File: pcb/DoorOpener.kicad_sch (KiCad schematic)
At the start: 8 parts, among them J1 Serial, SW1 POWER, SW2 Button, U2 ESP-01v090

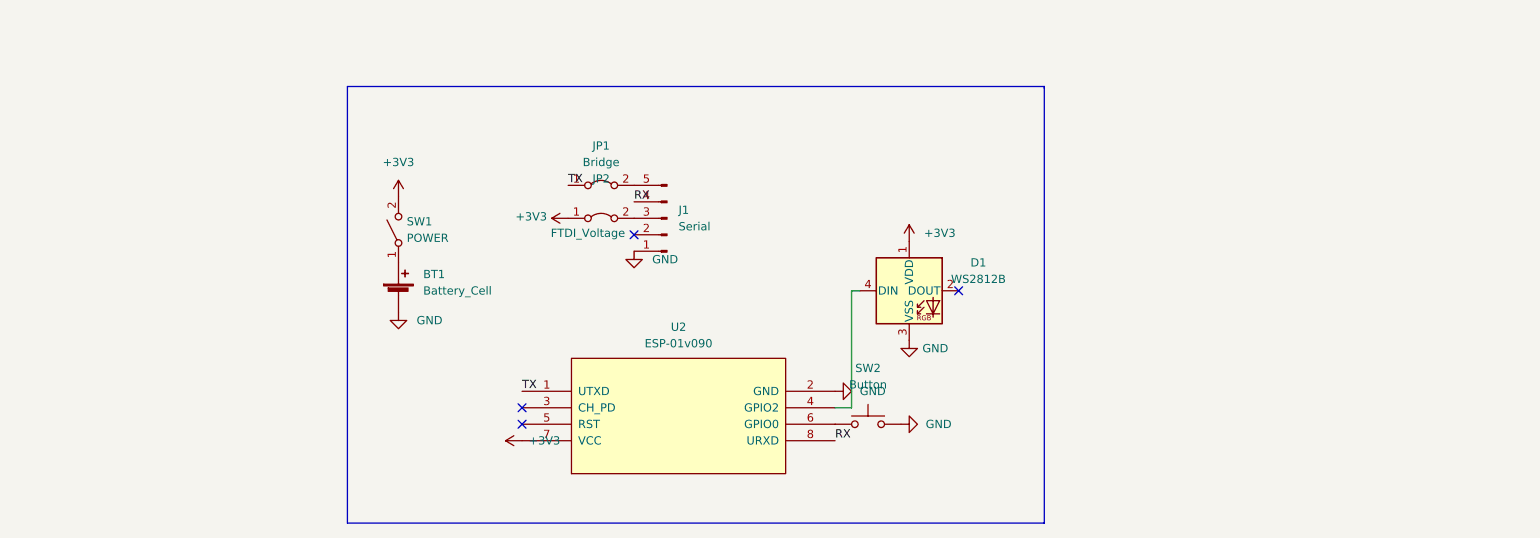
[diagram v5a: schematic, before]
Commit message: PCB: Add station module
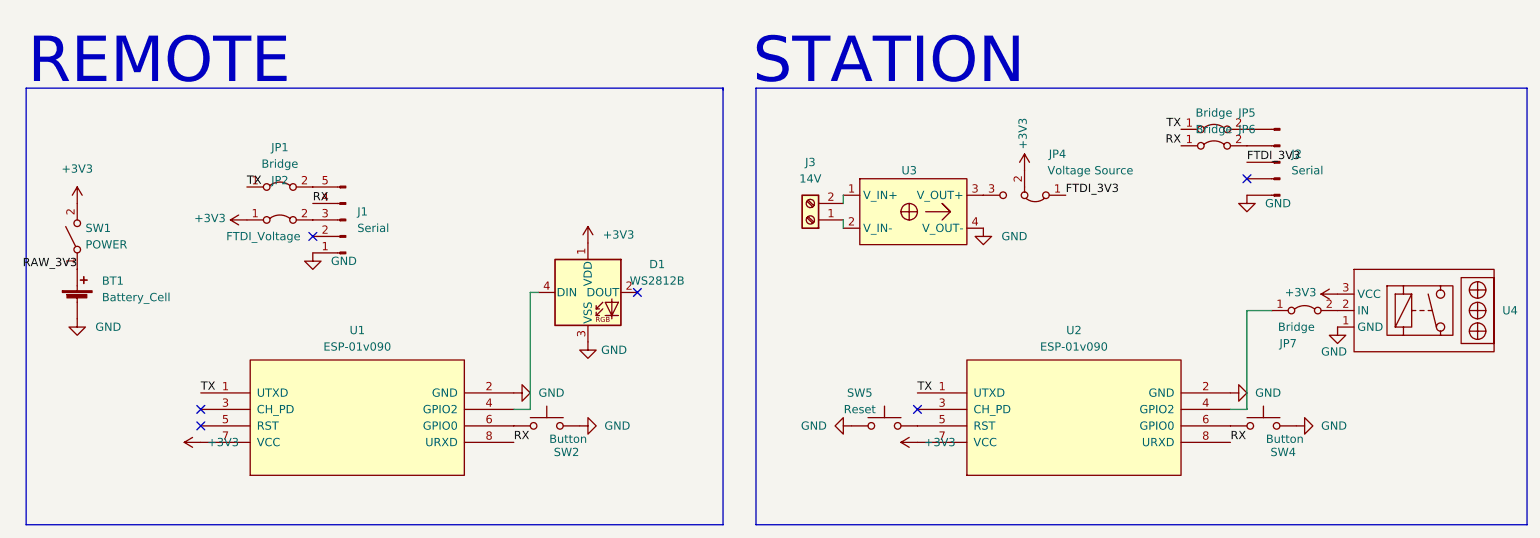
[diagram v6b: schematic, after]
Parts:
- added J2: Serial, Connector_PinHeader_2.54mm:PinHeader_1x05_P2.54mm_Horizontal, symbol Connector:Conn_01x05_Male
- added J3: 14V, TerminalBlock_Phoenix:TerminalBlock_Phoenix_MPT-0,5-2-2.54_1x02_P2.54mm_Horizontal, symbol Connector:Screw_Terminal_01x02
- added JP4: Voltage Source, Connector_PinHeader_2.54mm:PinHeader_1x03_P2.54mm_Vertical, symbol Jumper:Jumper_3_Bridged12
- added JP5, JP6, JP7: Bridge, Resistor_THT:R_Axial_DIN0204_L3.6mm_D1.6mm_P5.08mm_Horizontal, symbol Jumper:Jumper_2_Bridged
- added SW4: Button, Button_Switch_THT:SW_PUSH_6mm_H4.3mm, symbol Switch:SW_Push
- added SW5: Reset, Button_Switch_THT:SW_PUSH_6mm_H4.3mm, symbol Switch:SW_Push
- added U2: ESP-01v090, ESP8266:ESP-01, symbol ESP8266:ESP-01v090
- added U3: dcdc, dcdc:dcdc, symbol dcdc:dcdc
- added U4: relais_module, relais_module:relais_module, symbol relais_module:relais_module
- renumbered U2 to U1
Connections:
- net +3V3: now also JP4.2 (C), U2.7 (VCC), U4.3 (VCC)
- net GND: now also J2.1 (Pin_1), SW4.2, SW5.2, U2.2 (GND), U3.4 (V_OUT-), U4.1 (GND)
- net RX: now also JP6.1 (A), U2.8 (URXD)
- net TX: now also JP5.1 (A), U2.1 (UTXD)
- net RAW_3V3: now reaches BT1.1 (+), SW1.1 (A)
- new net: JP7.2 (B), U4.2 (IN)
- new net: JP7.1 (A), U2.4 (GPIO2)
- new net: SW4.1, U2.6 (GPIO0)
- new net: SW5.1, U2.5 (RST)
- new net: J2.5 (Pin_5), JP5.2 (B)
- new net: J3.1 (Pin_1), U3.2 (V_IN-)
- new net: J3.2 (Pin_2), U3.1 (V_IN+)
- new net: J2.4 (Pin_4), JP6.2 (B)
- new net: JP4.3 (B), U3.3 (V_OUT+)
- new net FTDI_3V3: J2.3 (Pin_3), JP4.1 (A)
- no-connect marks 4 -> 6
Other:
- note added: "REMOTE"
- note added: "STATION"
- moved on the sheet: BT1, D1, J1, JP1, JP2, SW1, SW2, U1

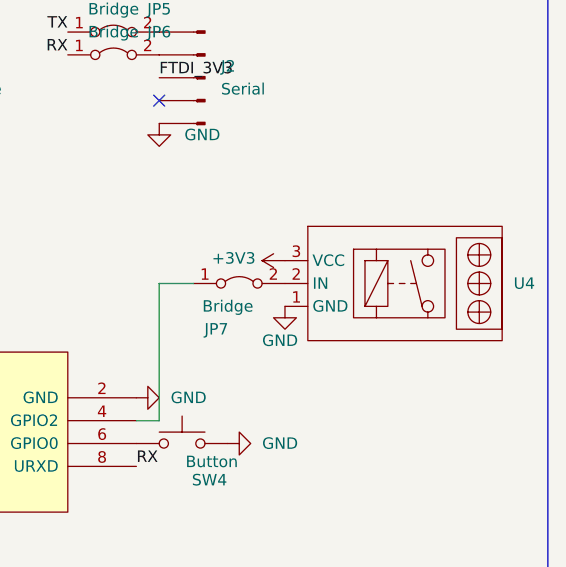
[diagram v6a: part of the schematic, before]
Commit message: Update terminal socket footprint and some minor changes
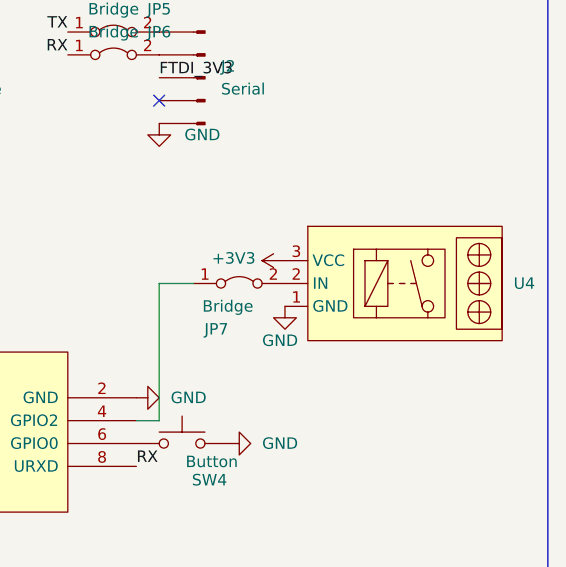
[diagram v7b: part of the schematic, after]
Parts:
- J3: footprint TerminalBlock_Phoenix:TerminalBlock_Phoenix_MPT-0,5-2-2.54_1x02_P2.54mm_Horizontal -> TerminalBlock_Phoenix:TerminalBlock_Phoenix_PT-1,5-2-3.5-H_1x02_P3.50mm_Horizontal
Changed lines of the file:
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@@
     (property "Reference" "J3" (id 0) (at 157.48 55.88 0))
     (property "Value" "14V" (id 1) (at 157.48 58.42 0))
-    (property "Footprint" "TerminalBlock_Phoenix:TerminalBlock_Phoenix_MPT-0,5-2-2.54_1x02_P2.54mm_Horizontal" (id 2) (at 157.48 64.77 0)
+    (property "Footprint" "TerminalBlock_Phoenix:TerminalBlock_Phoenix_PT-1,5-2-3.5-H_1x02_P3.50mm_Horizontal" (id 2) (at 157.48 64.77 0)
       (effects (font (size 1.27 1.27)) hide)
     )
@@
     )
     (path "/7b60c054-427f-4876-9763-2647089898cd"
-      (reference "J3") (unit 1) (value "14V") (footprint "TerminalBlock_Phoenix:TerminalBlock_Phoenix_MPT-0,5-2-2.54_1x02_P2.54mm_Horizontal")
+      (reference "J3") (unit 1) (value "14V") (footprint "TerminalBlock_Phoenix:TerminalBlock_Phoenix_PT-1,5-2-3.5-H_1x02_P3.50mm_Horizontal")
     )
     (path "/37204591-45c3-440b-a507-d0392365311c"

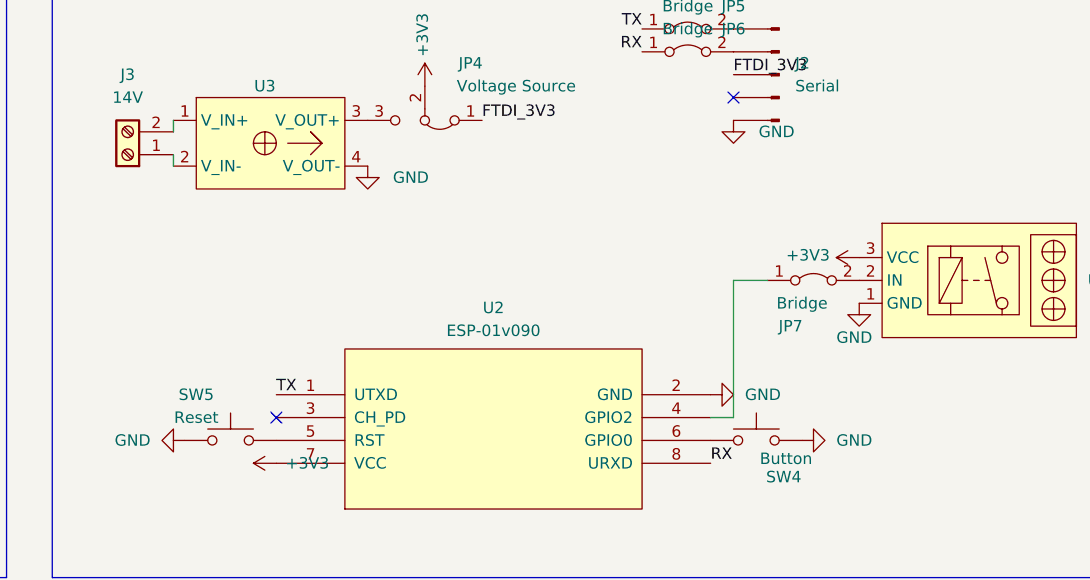
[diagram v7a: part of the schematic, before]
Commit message: Swap VCC and Signal pin
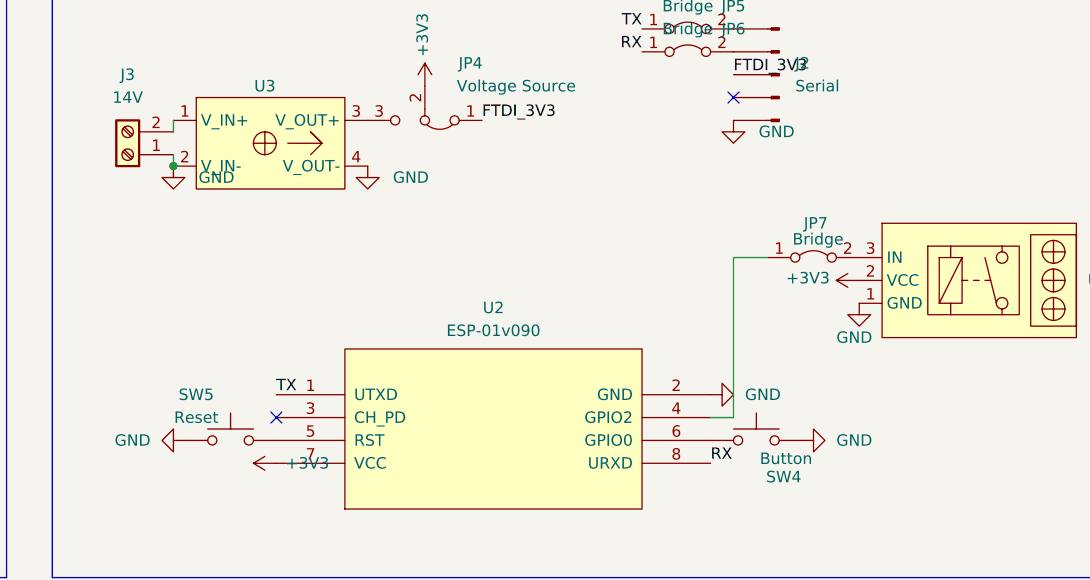
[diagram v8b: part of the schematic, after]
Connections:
- net +3V3: now also U4.2 (VCC); no longer U4.3 (VCC)
- net GND: now also J3.1 (Pin_1), U3.2 (V_IN-)
- net at JP7.2 (B): now also U4.3 (IN); no longer U4.2 (IN)
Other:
- moved on the sheet: JP7
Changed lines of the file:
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@@
     (rev "v0.2")
+  )
+  (junction (at 162.56 66.04) (diameter 0) (color 0 0 0 0)
   )
   (no_connect (at 130.81 75.946))
@@
     (stroke (width 0) (type default) (color 0 0 0 0))
   )
-  (wire (pts (xy 224.79 93.98) (xy 224.79 78.74))
+  (wire (pts (xy 224.79 76.2) (xy 224.79 93.98))
     (stroke (width 0) (type default) (color 0 0 0 0))
   )
@@
     (stroke (width 0) (type default) (color 0 0 0 0))
   )
-  (wire (pts (xy 224.79 78.74) (xy 228.6 78.74))
-    (stroke (width 0) (type default) (color 0 0 0 0))
-  )
   (wire (pts (xy 222.25 93.98) (xy 224.79 93.98))
     (stroke (width 0) (type default) (color 0 0 0 0))
   )
   (polyline (pts (xy 149.098 111.76) (xy 149.098 44.45))
+    (stroke (width 0) (type default) (color 0 0 0 0))
+  )
+  (wire (pts (xy 228.6 76.2) (xy 224.79 76.2))
     (stroke (width 0) (type default) (color 0 0 0 0))
   )
@@
     (pin "1")
   )
-  (symbol (lib_id "Jumper:Jumper_2_Bridged") (at 233.68 78.74 0) (unit 1)
-    (in_bom yes) (on_board yes)
-    (property "Reference" "JP7" (id 0) (at 231.14 83.82 0))
-    (property "Value" "Bridge" (id 1) (at 232.41 81.28 0))
-    (property "Footprint" "Resistor_THT:R_Axial_DIN0204_L3.6mm_D1.6mm_P5.08mm_Horizontal" (id 2) (at 233.68 78.74 0)
-      (effects (font (size 1.27 1.27)) hide)
-    )
-    (property "Datasheet" "~" (id 3) (at 233.68 78.74 0)
+  (symbol (lib_id "Jumper:Jumper_2_Bridged") (at 233.68 76.2 0) (unit 1)
+    (in_bom yes) (on_board yes)
+    (property "Reference" "JP7" (id 0) (at 233.934 72.39 0))
+    (property "Value" "Bridge" (id 1) (at 234.188 74.168 0))
+    (property "Footprint" "Resistor_THT:R_Axial_DIN0204_L3.6mm_D1.6mm_P5.08mm_Horizontal" (id 2) (at 233.68 76.2 0)
+      (effects (font (size 1.27 1.27)) hide)
+    )
+    (property "Datasheet" "~" (id 3) (at 233.68 76.2 0)
       (effects (font (size 1.27 1.27)) hide)
     )
@@
     (pin "1")
   )
+  (symbol (lib_id "power:GND") (at 162.56 66.04 0) (unit 1)
+    (in_bom yes) (on_board yes) (fields_autoplaced)
+    (property "Reference" "#PWR0113" (id 0) (at 162.56 72.39 0)
+      (effects (font (size 1.27 1.27)) hide)
+    )
+    (property "Value" "GND" (id 1) (at 165.354 67.3099 0)
+      (effects (font (size 1.27 1.27)) (justify left))
+    )
+    (property "Footprint" "" (id 2) (at 162.56 66.04 0)
+      (effects (font (size 1.27 1.27)) hide)
+    )
+    (property "Datasheet" "" (id 3) (at 162.56 66.04 0)
+      (effects (font (size 1.27 1.27)) hide)
+    )
+    (pin "1")
+  )
   (symbol (lib_id "Device:Battery_Cell") (at 44.45 77.47 0) (unit 1)
     (in_bom yes) (on_board yes) (fields_autoplaced)
@@
     (pin "1")
   )
-  (symbol (lib_id "power:+3V3") (at 238.76 76.2 90) (unit 1)
-    (in_bom yes) (on_board yes)
-    (property "Reference" "#PWR0119" (id 0) (at 242.57 76.2 0)
-      (effects (font (size 1.27 1.27)) hide)
-    )
-    (property "Value" "+3V3" (id 1) (at 230.632 75.946 90)
-      (effects (font (size 1.27 1.27)) (justify right))
-    )
-    (property "Footprint" "" (id 2) (at 238.76 76.2 0)
-      (effects (font (size 1.27 1.27)) hide)
-    )
-    (property "Datasheet" "" (id 3) (at 238.76 76.2 0)
+  (symbol (lib_id "power:+3V3") (at 238.76 78.74 90) (unit 1)
+    (in_bom yes) (on_board yes)
+    (property "Reference" "#PWR0119" (id 0) (at 242.57 78.74 0)
+      (effects (font (size 1.27 1.27)) hide)
+    )
+    (property "Value" "+3V3" (id 1) (at 230.632 78.486 90)
+      (effects (font (size 1.27 1.27)) (justify right))
+    )
+    (property "Footprint" "" (id 2) (at 238.76 78.74 0)
+      (effects (font (size 1.27 1.27)) hide)
+    )
+    (property "Datasheet" "" (id 3) (at 238.76 78.74 0)
       (effects (font (size 1.27 1.27)) hide)
     )
@@
       (reference "#PWR0112") (unit 1) (value "+3V3") (footprint "")
     )
+    (path "/d5d02e1f-c34a-4fe7-bb7d-b3d4113adc0b"
+      (reference "#PWR0113") (unit 1) (value "GND") (footprint "")
+    )
     (path "/4e56ab50-51d1-4e38-a894-8ac8b91920fb"
